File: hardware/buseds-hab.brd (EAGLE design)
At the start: 39 parts, among them IC1 MBED, Q1 MOSFET-NCHANNELPTH2, Q2 MOSFET-NCHANNELPTH2, U1 MCP1827-5002E/AT

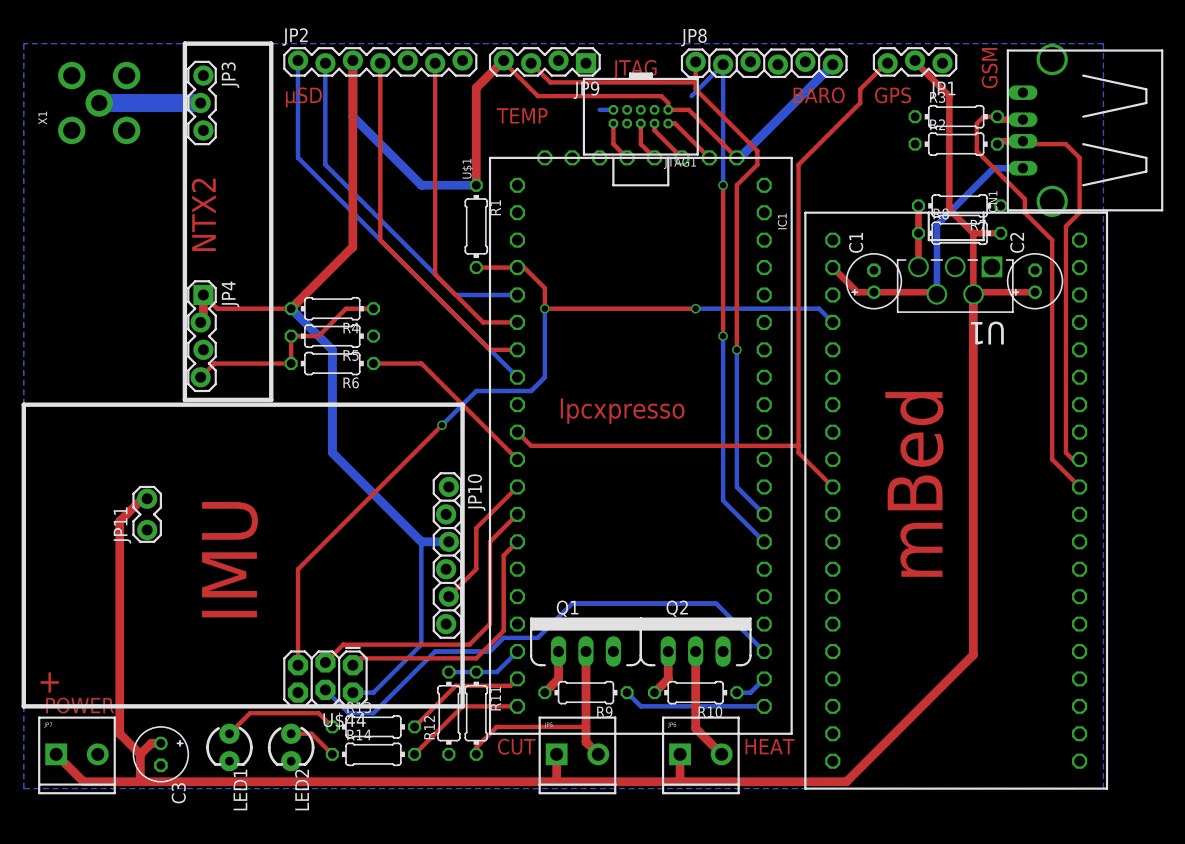
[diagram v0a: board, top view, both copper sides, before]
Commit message: Made space for voltage regulator tab
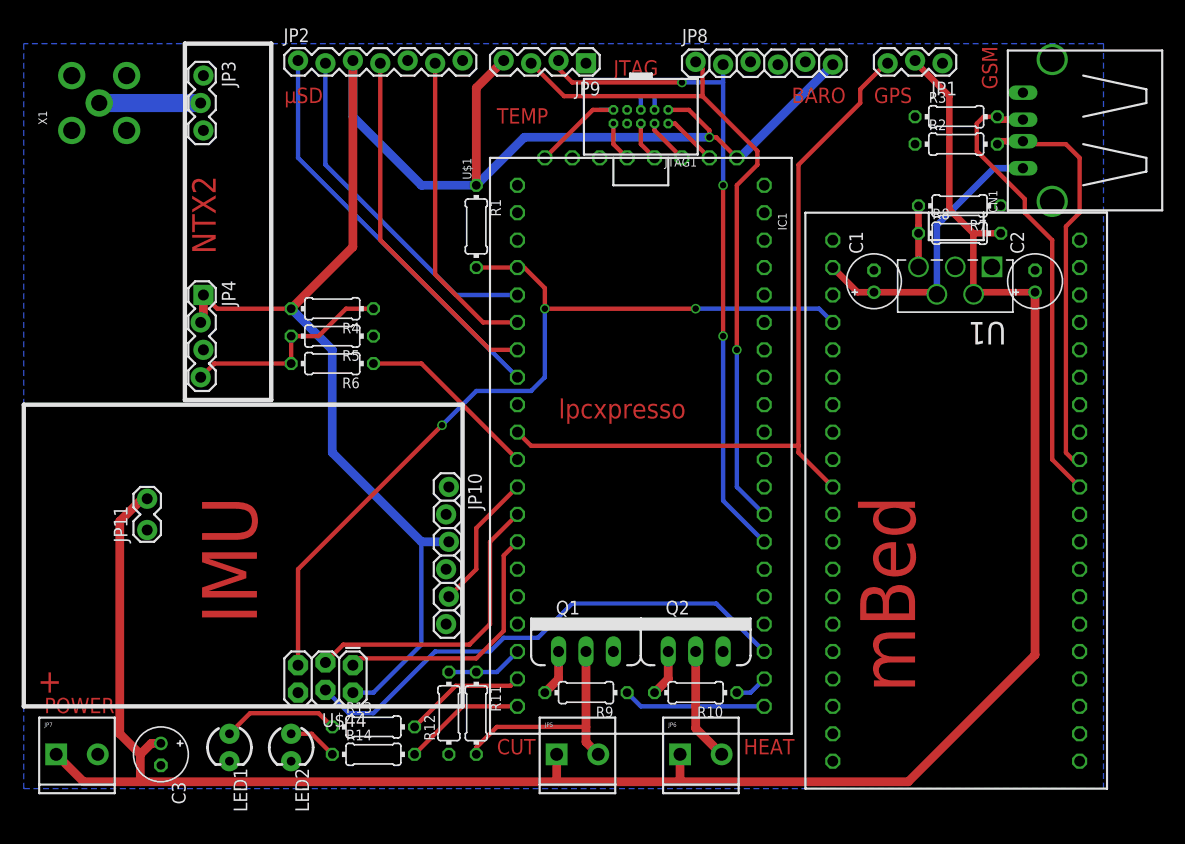
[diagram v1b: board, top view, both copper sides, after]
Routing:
- net SCL: track 50.7 -> 62.3 mm, vias 2 -> 3
- net GND: track 1.27 -> 12.0 mm
- net 3.3V: track 153.6 -> 160.0 mm, vias 0 -> 1
- net 5.0V: track 192.3 -> 198.2 mm
- net SDA: track 62.1 -> 63.3 mm
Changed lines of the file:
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@@
 <text x="66.675" y="3.175" size="1.4224" layer="1" font="vector" ratio="14">HEAT</text>
 <text x="43.815" y="3.175" size="1.4224" layer="1" font="vector" ratio="14">CUT</text>
-<text x="85.09" y="19.05" size="5.08" layer="1" font="vector" ratio="14" rot="R90">mBed</text>
+<text x="82.55" y="8.89" size="5.08" layer="1" font="vector" ratio="14" rot="R90">mBed</text>
 <text x="49.53" y="34.29" size="1.778" layer="1" font="vector" ratio="14">lpcxpresso</text>
 <text x="21.59" y="15.24" size="5.08" layer="1" font="vector" ratio="14" rot="R90">IMU</text>
@@
 <contactref element="LED2" pad="K"/>
 <wire x1="54.61" y1="62.865" x2="53.34" y2="62.865" width="0.4064" layer="16"/>
-<wire x1="57.15" y1="62.865" x2="58.42" y2="62.865" width="0" layer="19" extent="1-1"/>
-<wire x1="54.61" y1="62.865" x2="57.15" y2="62.865" width="0" layer="19" extent="1-1"/>
-<wire x1="52.07" y1="67.183" x2="53.34" y2="62.865" width="0" layer="19" extent="16-16"/>
+<wire x1="54.61" y1="62.865" x2="52.705" y2="62.865" width="0.4064" layer="1"/>
+<wire x1="52.705" y1="62.865" x2="48.26" y2="58.42" width="0.4064" layer="1"/>
+<wire x1="58.42" y1="62.865" x2="58.42" y2="64.135" width="0.4064" layer="16"/>
+<wire x1="57.15" y1="62.865" x2="57.15" y2="64.135" width="0.4064" layer="16"/>
 </signal>
 <signal name="TDO">
@@
 <contactref element="R4" pad="2"/>
 <wire x1="59.69" y1="62.865" x2="61.595" y2="62.865" width="0.4064" layer="1"/>
-<wire x1="61.595" y1="62.865" x2="66.04" y2="58.42" width="0.4064" layer="1"/>
 <contactref element="JP8" pad="6"/>
 <contactref element="JP9" pad="4"/>
@@
 <wire x1="24.765" y1="44.45" x2="30.48" y2="50.165" width="0.8128" layer="1"/>
 <wire x1="30.48" y1="50.165" x2="30.48" y2="67.437" width="0.8128" layer="1"/>
-<wire x1="59.69" y1="62.865" x2="59.69" y2="63.5" width="0.4064" layer="1"/>
-<wire x1="59.69" y1="63.5" x2="59.055" y2="64.135" width="0.4064" layer="1"/>
 <wire x1="74.93" y1="67.056" x2="66.294" y2="58.42" width="0.8128" layer="16"/>
 <wire x1="66.294" y1="58.42" x2="66.04" y2="58.42" width="0.8128" layer="16"/>
@@
 <wire x1="28.575" y1="31.115" x2="36.83" y2="22.86" width="0.8128" layer="16"/>
 <wire x1="36.83" y1="22.86" x2="39.37" y2="22.86" width="0.8128" layer="16"/>
-<wire x1="59.055" y1="64.135" x2="47.625" y2="64.135" width="0.4064" layer="1"/>
-<wire x1="47.625" y1="64.135" x2="44.45" y2="67.31" width="0.4064" layer="1"/>
 <wire x1="44.45" y1="67.31" x2="44.45" y2="67.437" width="0.4064" layer="1"/>
 <wire x1="41.91" y1="55.88" x2="41.91" y2="64.897" width="0.8128" layer="1"/>
 <wire x1="41.91" y1="64.897" x2="44.45" y2="67.437" width="0.8128" layer="1"/>
+<wire x1="46.355" y1="60.325" x2="63.5" y2="60.325" width="0.8128" layer="16"/>
+<wire x1="46.355" y1="60.325" x2="41.91" y2="55.88" width="0.8128" layer="16"/>
+<via x="63.5" y="60.325" extent="1-16" drill="0.6"/>
+<wire x1="61.595" y1="62.865" x2="63.5" y2="60.96" width="0.4064" layer="1"/>
+<wire x1="63.5" y1="60.96" x2="63.5" y2="60.325" width="0.4064" layer="1"/>
+<wire x1="66.04" y1="58.42" x2="64.135" y2="60.325" width="0.4064" layer="1"/>
+<wire x1="64.135" y1="60.325" x2="63.5" y2="60.325" width="0.4064" layer="1"/>
 </signal>
 <signal name="D-">
@@
 <wire x1="11.811" y1="4.191" x2="10.795" y2="3.175" width="0.8128" layer="1"/>
 <wire x1="10.795" y1="3.175" x2="10.795" y2="0.635" width="0.8128" layer="1"/>
-<wire x1="87.9475" y1="45.8089" x2="87.9475" y2="12.3825" width="0.8128" layer="1"/>
-<wire x1="87.9475" y1="12.3825" x2="76.2" y2="0.635" width="0.8128" layer="1"/>
-<wire x1="76.2" y1="0.635" x2="60.7822" y2="0.635" width="0.8128" layer="1"/>
+<wire x1="93.6625" y1="12.3825" x2="81.915" y2="0.635" width="0.8128" layer="1"/>
+<wire x1="81.915" y1="0.635" x2="60.7822" y2="0.635" width="0.8128" layer="1"/>
 <wire x1="10.9728" y1="26.8478" x2="8.89" y2="24.765" width="0.8128" layer="1"/>
 <wire x1="8.89" y1="24.765" x2="8.89" y2="5.08" width="0.8128" layer="1"/>
@@
 <wire x1="82.55" y1="67.437" x2="82.55" y2="67.31" width="0.6096" layer="1"/>
 <wire x1="82.55" y1="67.31" x2="85.725" y2="64.135" width="0.6096" layer="1"/>
+<wire x1="93.6625" y1="45.974" x2="93.6625" y2="12.3825" width="0.8128" layer="1"/>
 </signal>
 <signal name="GPS_DATA">
@@
 <wire x1="66.04" y1="55.88" x2="67.945" y2="57.785" width="0.4064" layer="1"/>
 <wire x1="67.945" y1="57.785" x2="67.945" y2="59.055" width="0.4064" layer="1"/>
-<wire x1="67.945" y1="59.055" x2="62.23" y2="64.77" width="0.4064" layer="1"/>
-<wire x1="62.23" y1="64.77" x2="62.23" y2="65.405" width="0.4064" layer="1"/>
-<wire x1="62.23" y1="65.405" x2="62.23" y2="67.31" width="0.4064" layer="1"/>
-<wire x1="46.99" y1="67.183" x2="48.768" y2="65.405" width="0.4064" layer="1"/>
-<wire x1="48.768" y1="65.405" x2="62.23" y2="65.405" width="0.4064" layer="1"/>
+<wire x1="67.945" y1="59.055" x2="62.865" y2="64.135" width="0.4064" layer="1"/>
+<wire x1="62.865" y1="64.135" x2="62.865" y2="66.675" width="0.4064" layer="1"/>
+<wire x1="62.865" y1="66.675" x2="62.23" y2="67.31" width="0.4064" layer="1"/>
+<wire x1="46.99" y1="67.183" x2="50.038" y2="64.135" width="0.4064" layer="1"/>
+<wire x1="50.038" y1="64.135" x2="62.865" y2="64.135" width="0.4064" layer="1"/>
 </signal>
 <signal name="SCL">
@@
 <contactref element="JP9" pad="2"/>
 <contactref element="U$1" pad="27"/>
-<wire x1="52.07" y1="64.135" x2="61.849" y2="64.135" width="0" layer="19" extent="1-16"/>
-<wire x1="61.849" y1="64.135" x2="64.77" y2="67.056" width="0.4064" layer="16"/>
 <wire x1="68.58" y1="22.86" x2="64.77" y2="26.67" width="0.4064" layer="16"/>
 <wire x1="64.77" y1="26.67" x2="64.77" y2="41.91" width="0.4064" layer="16"/>
@@
 <wire x1="64.77" y1="41.91" x2="64.77" y2="55.88" width="0.4064" layer="1"/>
 <via x="64.77" y="55.88" extent="1-16" drill="0.6"/>
-<wire x1="64.77" y1="55.88" x2="64.77" y2="67.056" width="0.4064" layer="16"/>
-<wire x1="52.07" y1="64.135" x2="49.53" y2="66.675" width="0" layer="19" extent="1-16"/>
-<wire x1="49.53" y1="66.675" x2="49.53" y2="67.437" width="0.4064" layer="16"/>
+<wire x1="64.77" y1="55.88" x2="64.77" y2="65.405" width="0.4064" layer="16"/>
+<wire x1="64.77" y1="65.405" x2="64.77" y2="67.056" width="0.4064" layer="16"/>
+<wire x1="49.53" y1="67.437" x2="49.53" y2="66.675" width="0.4064" layer="1"/>
+<wire x1="49.53" y1="66.675" x2="50.8" y2="65.405" width="0.4064" layer="1"/>
+<wire x1="50.8" y1="65.405" x2="60.96" y2="65.405" width="0.4064" layer="1"/>
+<via x="60.96" y="65.405" extent="1-16" drill="0.6"/>
+<wire x1="60.96" y1="65.405" x2="64.77" y2="65.405" width="0.4064" layer="16"/>
 </signal>
 <signal name="IMU-SSEL">
